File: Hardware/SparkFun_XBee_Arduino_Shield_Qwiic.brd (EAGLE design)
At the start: 53.3 x 59.7 mm, 168 parts, among them J4 QWIIC_RIGHT_ANGLE, Q1 220mA/50V/3.5Ω, Q3 3.1A/30V/105mΩ, Q5 20V/4.2A/52mΩ/1.4W, U1 FSUSB30MUX_MSOP10, U2 AP63203, U3 ESD Diode, U4 FT231XS, U5 ESD Diode, X1 JUMPER-SMT_2_NO_SILK

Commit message: Adds Gerbers, updates ordering instructions to include material
* Fixes "Off" and "On" silk on switch
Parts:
- moved U$69 2.54 mm to (41.8, 25.5)
- moved U$46 2.54 mm to (42.2, 22.9)
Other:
- board text added: "Material: FR4: TG135-140"
- board text added: "Red Soldermask"
- board text added: "White Silk"
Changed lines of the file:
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@@
 <setting verticaltext="up"/>
 </settings>
-<grid distance="0.05" unitdist="inch" unit="inch" style="dots" multiple="1" display="yes" altdistance="0.002" altunitdist="inch" altunit="inch"/>
+<grid distance="0.05" unitdist="inch" unit="inch" style="dots" multiple="1" display="yes" altdistance="0.005" altunitdist="inch" altunit="inch"/>
 <layers>
 <layer number="1" name="Top" color="4" fill="1" visible="yes" active="yes"/>
@@
 <layer number="27" name="tValues" color="7" fill="1" visible="no" active="yes"/>
 <layer number="28" name="bValues" color="7" fill="1" visible="no" active="yes"/>
-<layer number="29" name="tStop" color="7" fill="3" visible="yes" active="yes"/>
+<layer number="29" name="tStop" color="7" fill="3" visible="no" active="yes"/>
 <layer number="30" name="bStop" color="7" fill="6" visible="no" active="yes"/>
 <layer number="31" name="tCream" color="7" fill="4" visible="no" active="yes"/>
@@
 <layer number="45" name="Holes" color="7" fill="1" visible="yes" active="yes"/>
 <layer number="46" name="Milling" color="3" fill="1" visible="no" active="yes"/>
-<layer number="47" name="Measures" color="7" fill="1" visible="yes" active="yes"/>
+<layer number="47" name="Measures" color="7" fill="1" visible="no" active="yes"/>
 <layer number="48" name="Document" color="7" fill="1" visible="no" active="yes"/>
 <layer number="49" name="Reference" color="13" fill="1" visible="yes" active="yes"/>
@@
 <dimension x1="50.8" y1="19.05" x2="50.8" y2="36.83" x3="60.96" y3="27.94" textsize="1.778" textratio="15" layer="47" unit="inch"/>
 <dimension x1="15.24" y1="59.69" x2="11.43" y2="57.15" x3="-3.81" y3="58.42" textsize="1.778" textratio="15" layer="47" dtype="vertical" unit="inch"/>
+<text x="78.74" y="22.86" size="1.778" layer="51" font="vector" ratio="15">Red Soldermask</text>
+<text x="78.74" y="19.05" size="1.778" layer="51" font="vector" ratio="15">White Silk</text>
+<text x="78.74" y="15.24" size="1.778" layer="51" font="vector" ratio="15">Material: FR4: TG135-140</text>
 </plain>
 <attributes>
@@
 <element name="U$41" library="topmirror" package="#GND#0" value="" x="48.1076" y="34.2392" smashed="yes"/>
 <element name="U$44" library="top" package="#3V3#1" value="" x="45.72" y="19.939" smashed="yes"/>
-<element name="U$69" library="pot" package="OFF311" value="" x="41.783" y="22.9108" smashed="yes"/>
+<element name="U$69" library="pot" package="OFF311" value="" x="41.783" y="25.4508" smashed="yes"/>
 <element name="U$52" library="top" package="#PLED#20" value="" x="45.5168" y="2.9972" smashed="yes" rot="MR0"/>
 <element name="U$93" library="pot" package="#IOLED#5" value="" x="47.0662" y="10.0584" smashed="yes" rot="MR0"/>
@@
 <element name="U$42" library="bot" package="#D0#3" value="" x="4.6736" y="22.8092" smashed="yes"/>
 <element name="U$43" library="bot" package="#X1#10" value="" x="43.18" y="30.6832" smashed="yes" rot="R90"/>
-<element name="U$46" library="bot" package="ON38" value="" x="42.2148" y="25.4" smashed="yes"/>
+<element name="U$46" library="bot" package="ON38" value="" x="42.2148" y="22.86" smashed="yes"/>
 <element name="U$53" library="topmirror" package="#GND#0" value="" x="48.1584" y="34.2392" smashed="yes" rot="MR0"/>
 <element name="U$63" library="topmirror" package="#GND#0" value="" x="48.133" y="31.7246" smashed="yes" rot="MR0"/>

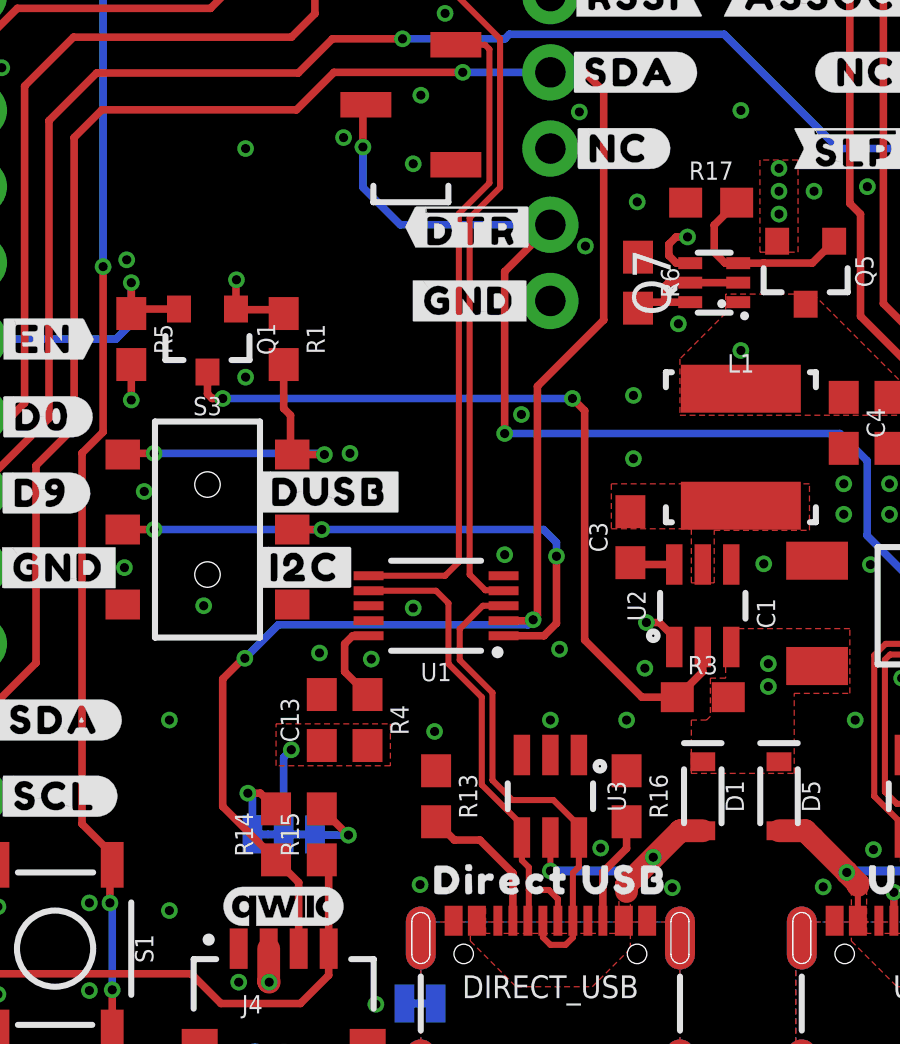
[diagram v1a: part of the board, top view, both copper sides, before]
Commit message: Replaces old USB mux switch with new one
* Removes 100Ohm resistor on VCC line
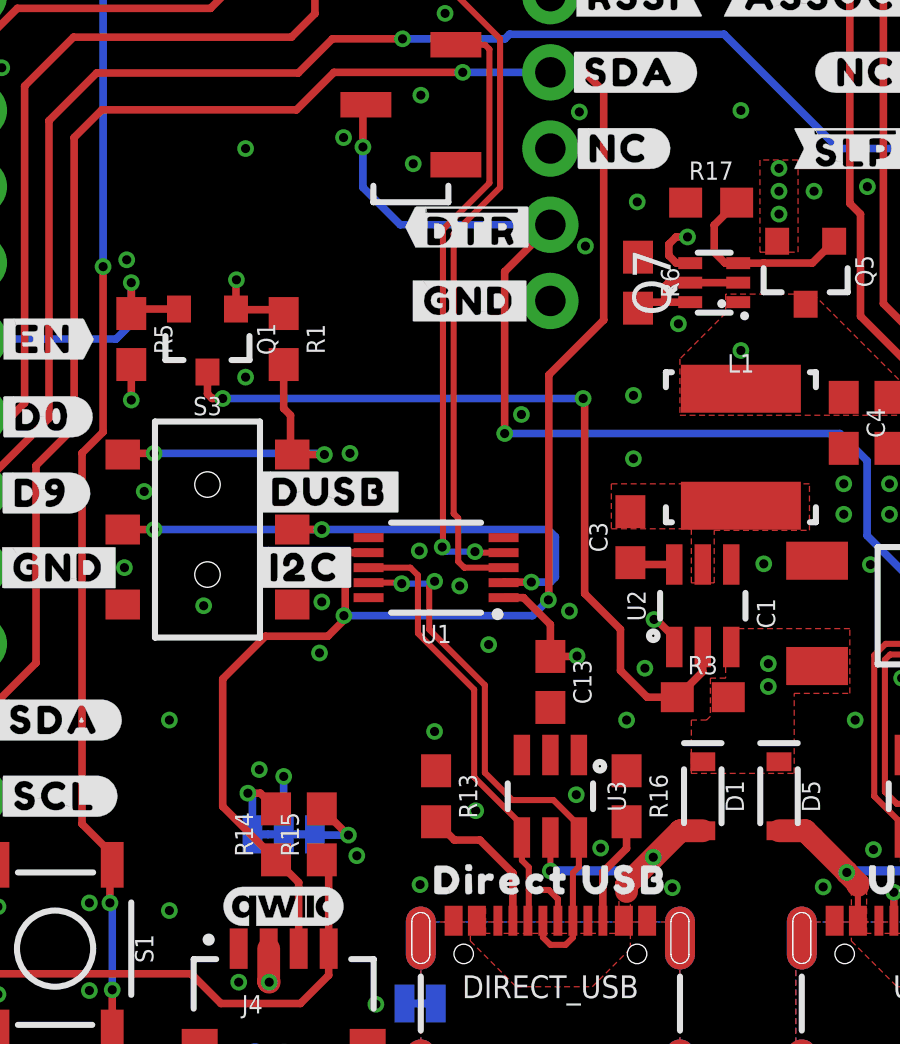
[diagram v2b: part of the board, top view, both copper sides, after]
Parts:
- removed R4: 100, SparkFun-Resistors:0603
- U1: value FSUSB30MUX_MSOP10 -> FSUSB42MUX
- moved C13 7.73 mm to (21.6, 14.0), turned to 270 degrees
- moved U1 1.27 mm to (17.8, 17.8)
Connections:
- removed net N$10: R4.1, U1.10
- net 3.3V: now also U1.1; no longer R4.2
- net D11/SDA: now also U1.7; no longer U1.2
- net DIRECT_D+: now also U1.9; no longer U1.3
- net DIRECT_D-: now also U1.8; no longer U1.7
- net DIRECT_SELECT: now also U1.2; no longer U1.1
- net GND: now also U1.10; no longer U1.9
- net XBEE_D+/SDA: now also U1.3; no longer U1.4
- net XBEE_D-: now also U1.4; no longer U1.6
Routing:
- net N$10: track 2.92 -> 0.00 mm
- net 3.3V: track 20.5 -> 23.4 mm, vias 14 -> 15
- net DIRECT_D+: track 16.4 -> 18.9 mm, vias 0 -> 2
- net D11/SDA: track 80.3 -> 82.2 mm
- net DIRECT_SELECT: track 20.2 -> 18.7 mm
- net XBEE_D-: track 21.9 -> 20.5 mm, vias 0 -> 2
- net 3.3V_VREG: track 13.2 -> 12.7 mm
- net GND: vias 113 -> 117

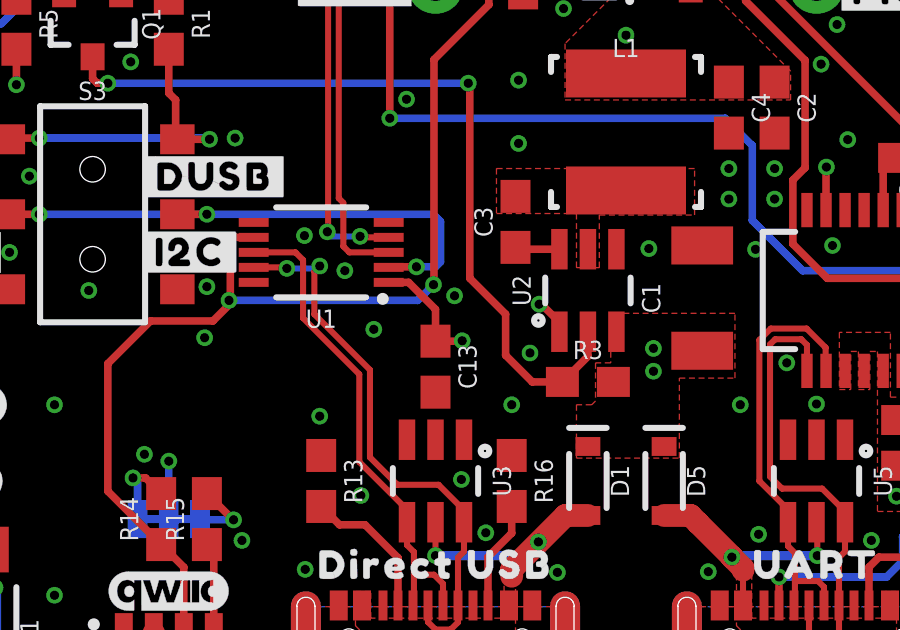
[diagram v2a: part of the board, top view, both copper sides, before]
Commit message: Small adjustment to design file after approving proximity DRC error
* Remakes panels
* Deletes old library
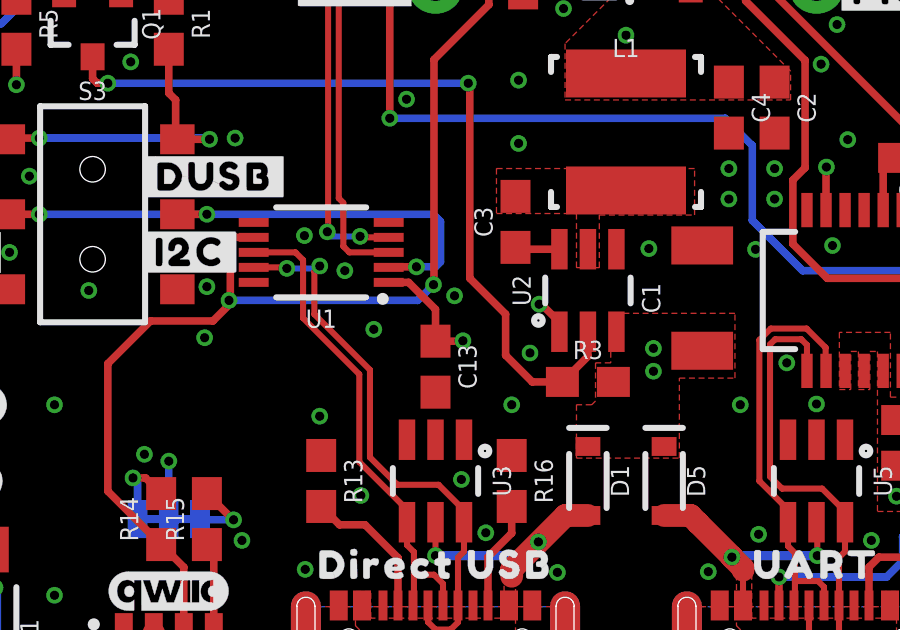
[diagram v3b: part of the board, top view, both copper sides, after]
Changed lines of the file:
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@@
 <drawing>
 <settings>
-<setting alwaysvectorfont="yes"/>
+<setting alwaysvectorfont="no"/>
 <setting verticaltext="up"/>
 </settings>
@@
 <wire x1="23.368" y1="33.655" x2="23.368" y2="26.035" width="0.254" layer="1"/>
 <via x="21.5232" y="16.7038" extent="1-16" drill="0.3048"/>
-<wire x1="21.5232" y1="16.7038" x2="21.4898" y2="16.6704" width="0.254" layer="1"/>
 <wire x1="21.5232" y1="16.7038" x2="21.5392" y2="16.7198" width="0.254" layer="1"/>
 <wire x1="21.5392" y1="16.7198" x2="21.5392" y2="24.2062" width="0.254" layer="1"/>
@@
 <wire x1="21.59" y1="14.82" x2="21.59" y2="15.88265625" width="0.254" layer="1"/>
 <wire x1="20.03" y1="16.78" x2="20.69265625" y2="16.78" width="0.254" layer="1"/>
-<wire x1="21.59" y1="14.82" x2="22.4654" y2="14.82" width="0.254" layer="1"/>
-<wire x1="22.4654" y1="14.82" x2="22.479" y2="14.8336" width="0.254" layer="1"/>
-<via x="22.479" y="14.8336" extent="1-16" drill="0.3048"/>
+<wire x1="21.59" y1="14.82" x2="22.4908" y2="14.82" width="0.254" layer="1"/>
+<wire x1="22.4908" y1="14.82" x2="22.5044" y2="14.8336" width="0.254" layer="1"/>
+<via x="22.5044" y="14.8336" extent="1-16" drill="0.3048"/>
 </signal>
 <signal name="N$11">
